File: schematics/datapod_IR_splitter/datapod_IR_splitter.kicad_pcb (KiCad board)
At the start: 2 copper layers, 66 x 81.3 mm, 9 parts, among them J1 DB9_Female_MountingHoles, J2 DB9_Male_MountingHoles, J3 DB9_Male_MountingHoles, J4 DB9_Male_MountingHoles, J5 DB9_Male_MountingHoles

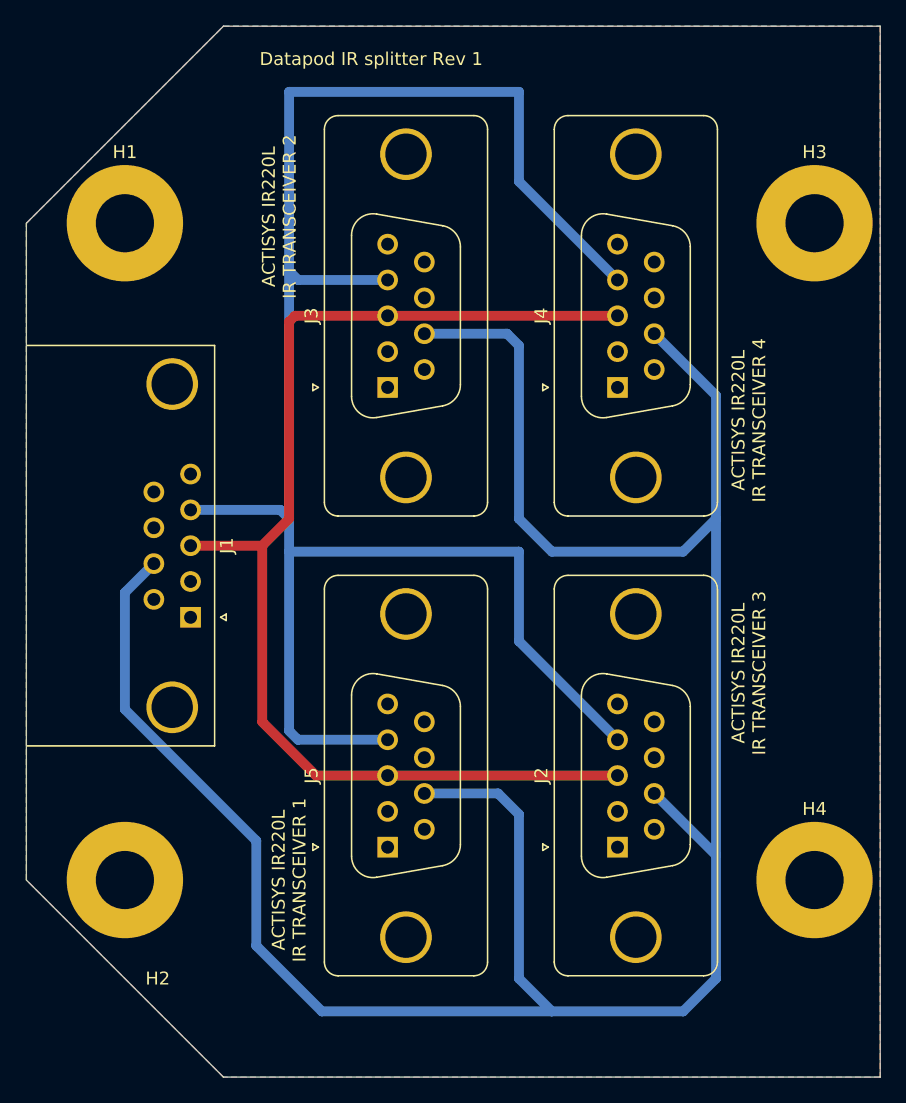
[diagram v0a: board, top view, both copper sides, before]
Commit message: increased distance between db9 connectors and added notes to transfer file with rx on the terminal
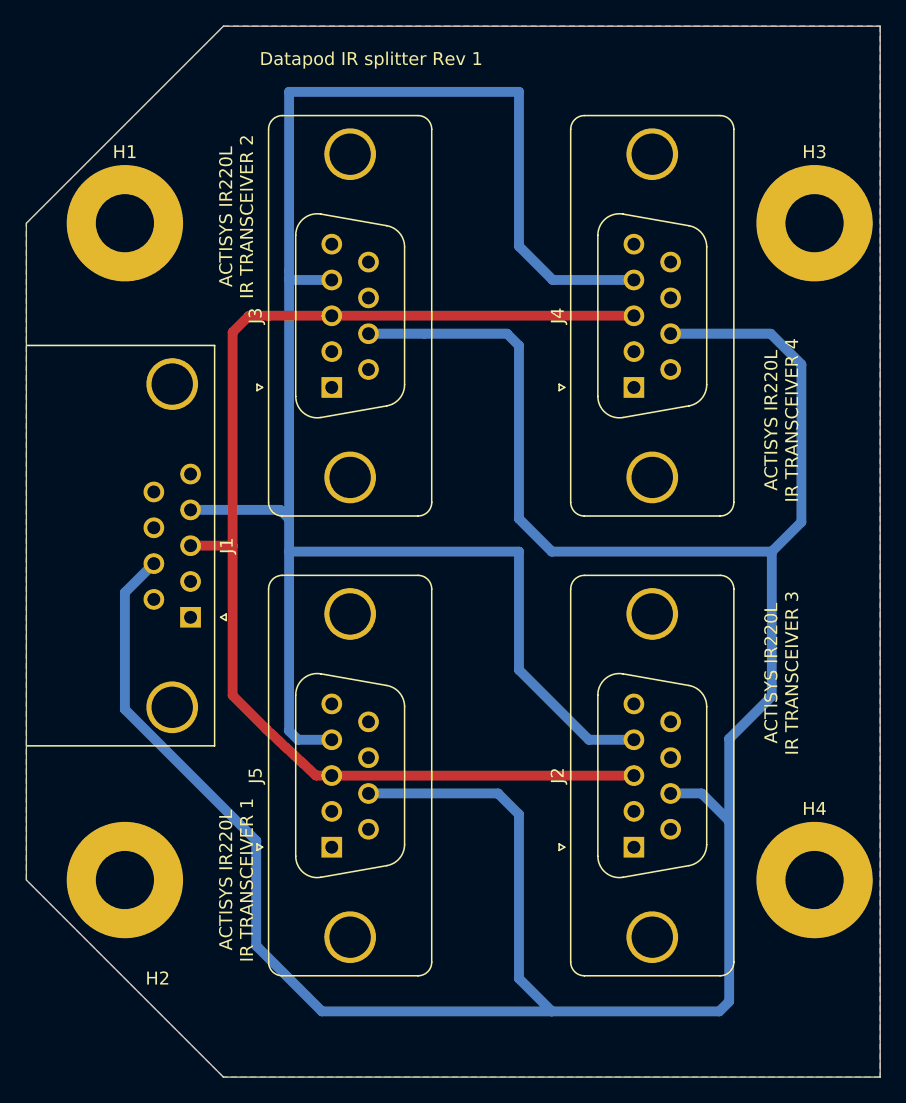
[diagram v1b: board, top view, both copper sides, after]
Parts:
- moved J3 4.32 mm to (130.3, 94.0)
- moved J5 4.32 mm to (130.3, 129.5)
- moved J2 1.27 mm to (153.7, 129.5)
- moved J4 1.27 mm to (153.7, 94.0)
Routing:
- net Net-(J1-Pad7): track 194.7 -> 216.4 mm
- net Net-(J1-Pad3): track 92.1 -> 96.4 mm
- net Net-(J1-Pad4): track 144.1 -> 142.0 mm
